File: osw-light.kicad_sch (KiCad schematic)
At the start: 53 parts, among them J2 USB_C_Receptacle_USB2.0, Q1 2N7002, SW1 SW_Push, SW2 SW_Push, SW4 SW_Push, SW5 SW_Push, U1 RV-8523-C3, U10 XC6209, U13 XC6209, U2 BMA400, U3 ESP32-PICO-MINI-02, U4 GC9A01_IPS_display, U5 BQ24230RGT, U6 CH340E, U7 LSM303C

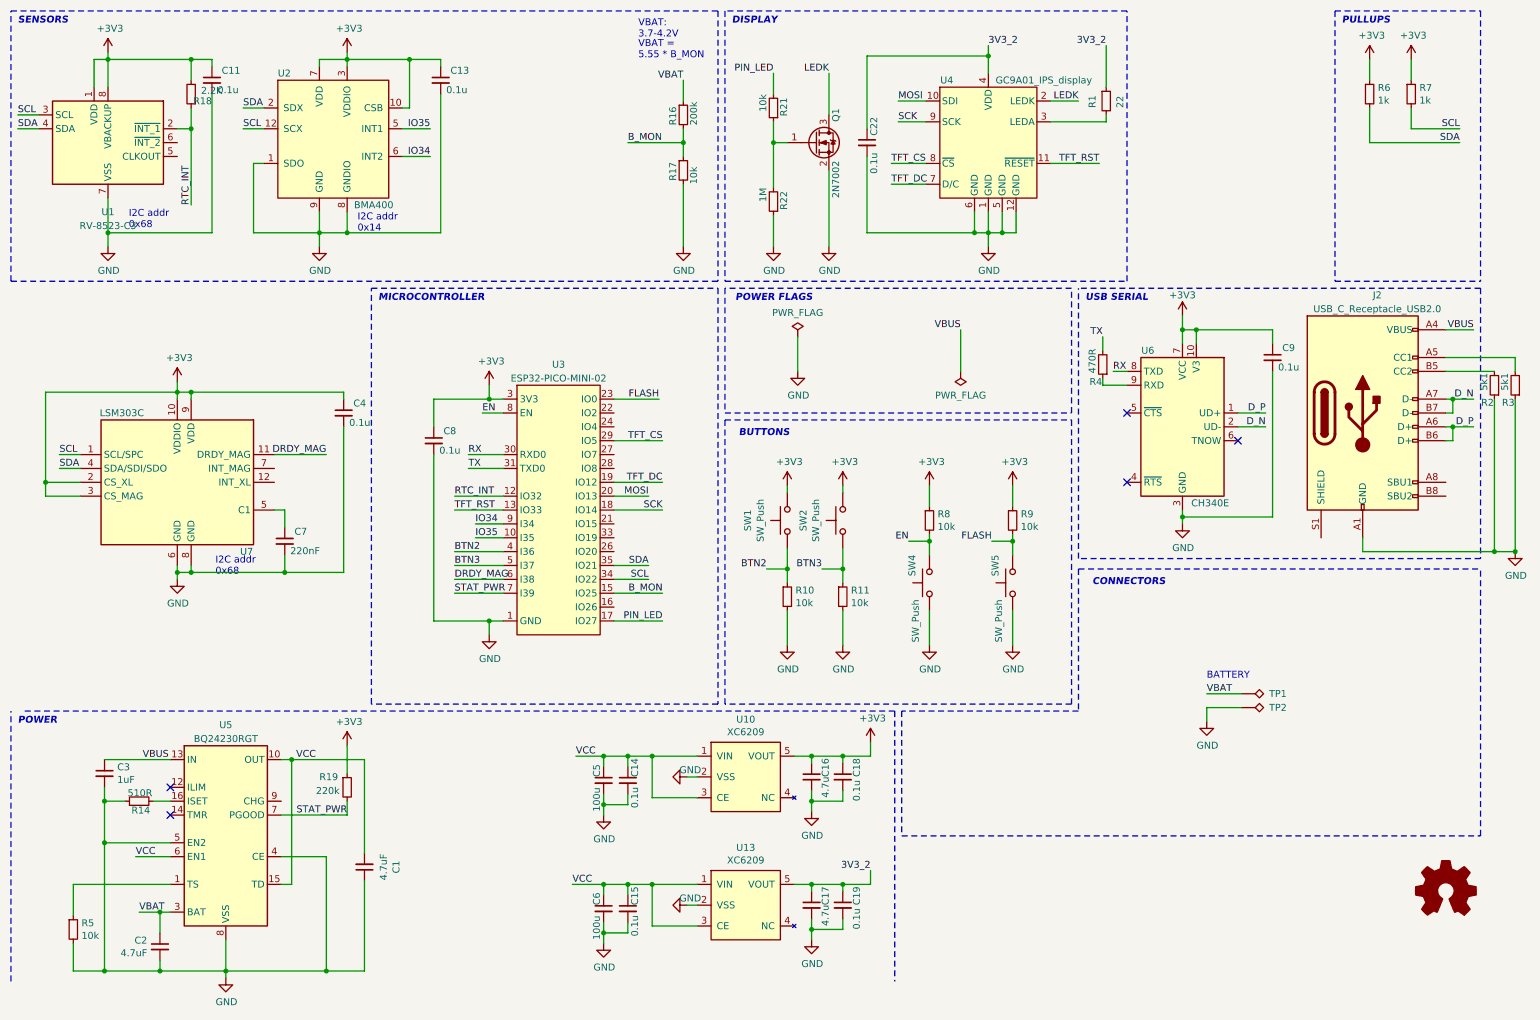
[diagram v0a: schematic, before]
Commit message: Fixed silkscreens. Replaced duplicate sensor with temperature sensor
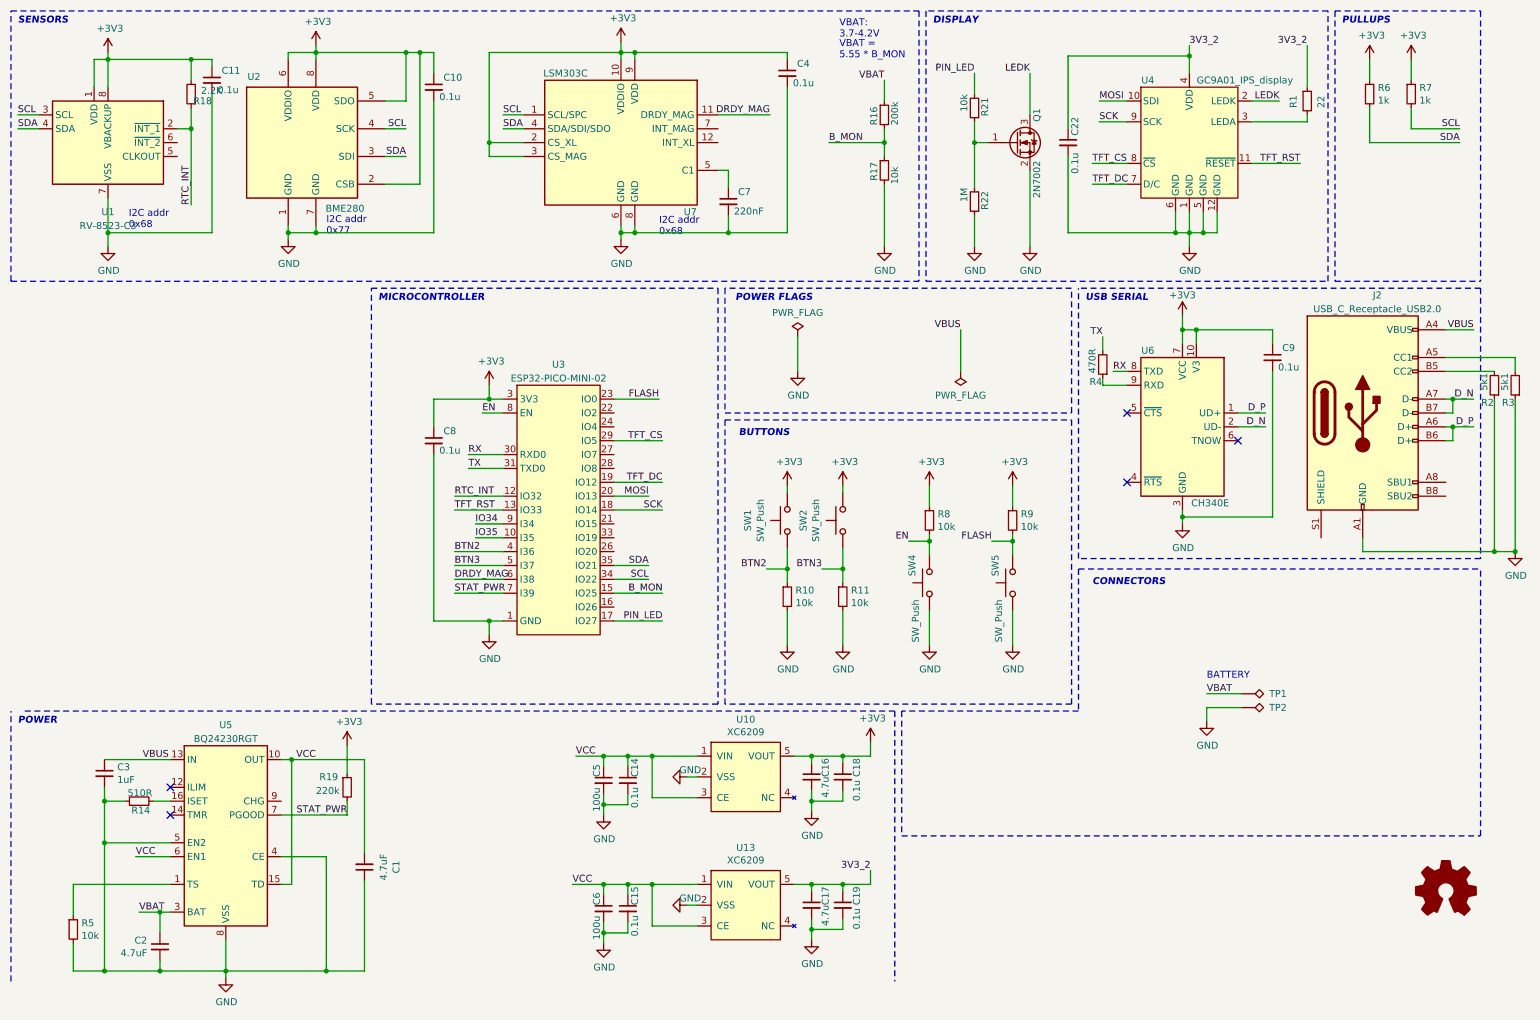
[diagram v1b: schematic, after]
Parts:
- removed C13: 0.1u, Capacitor_SMD:C_0603_1608Metric, symbol Device:C_Small
- removed U2: BMA400, open-Smartwatch:LGA-12_2x2mm_P0.5mm, symbol open-Smartwatch:BMA400
- added C10: 0.1u, Capacitor_SMD:C_0603_1608Metric, symbol Device:C_Small
- added U2: BME280, Package_LGA:Bosch_LGA-8_2.5x2.5mm_P0.65mm_ClockwisePinNumbering, symbol Sensor:BME280
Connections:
- net +3V3: now also C10.1, U2.2 (CSB), U2.5 (SDO), U2.6 (VDDIO), U2.8 (VDD)
- net GND: now also C10.2, U2.1 (GND), U2.7 (GND)
- net SCL: now also U2.4 (SCK)
- net SDA: now also U2.3 (SDI)
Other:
- note added: "I2C addr 0x77"
- note removed: "I2C addr 0x14"
- moved on the sheet: C22, C4, C7, Q1, R1, R16, R17, R21, R22, U4, U7

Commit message: Another commit. Removed gerbers as part of a git release
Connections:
- no-connect marks 5 -> 12
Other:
- moved on the sheet: J2, R2, R3, TP1, TP2
